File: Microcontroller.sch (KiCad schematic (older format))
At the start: 29 parts, among them J3 USB_B, J4 SWD, J5 DEBUG, U3 STM32F401VETx, U4 USBUF02W6, Y1 8MHz

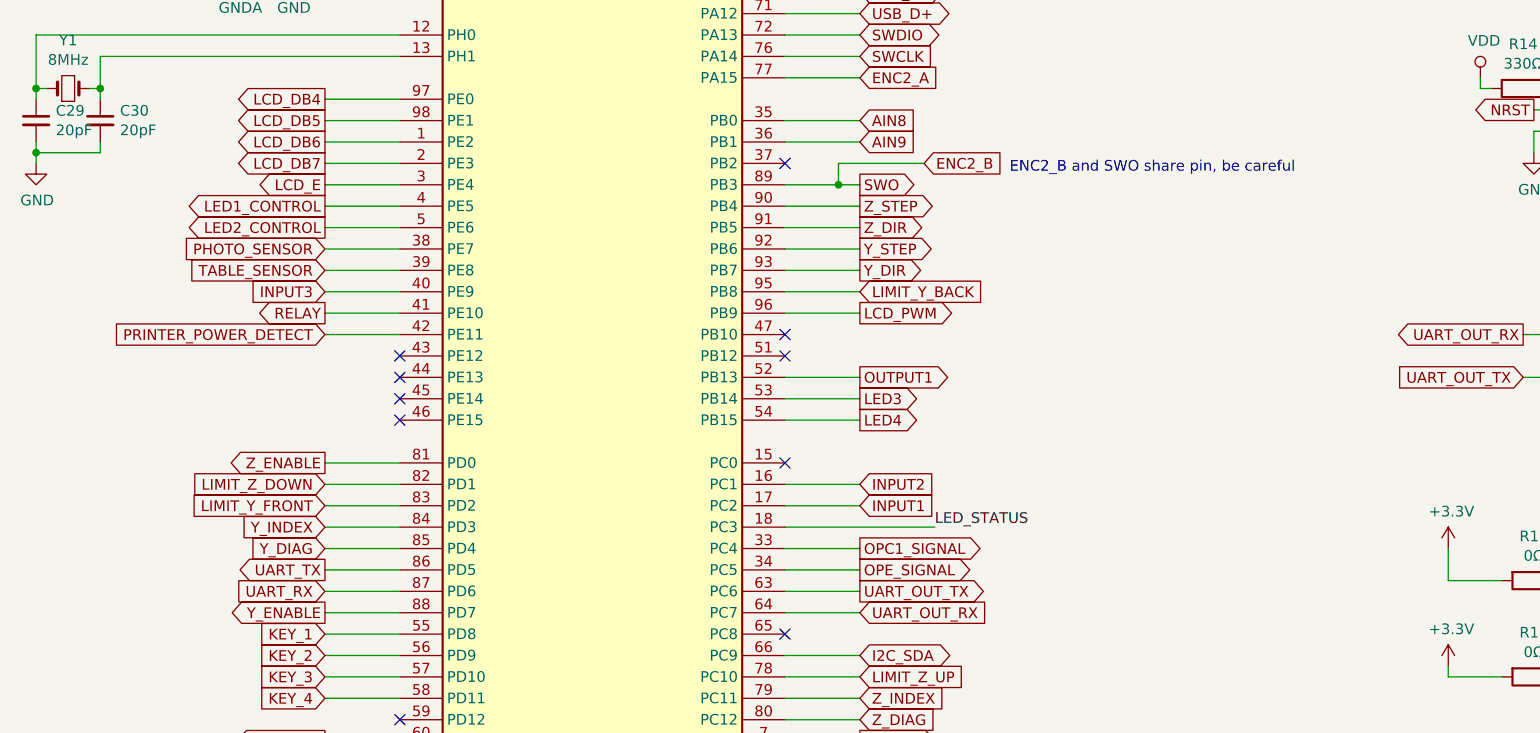
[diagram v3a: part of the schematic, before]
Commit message: Routing emergnency, photo barier, relay, voltage detect, analog, footprint improvment
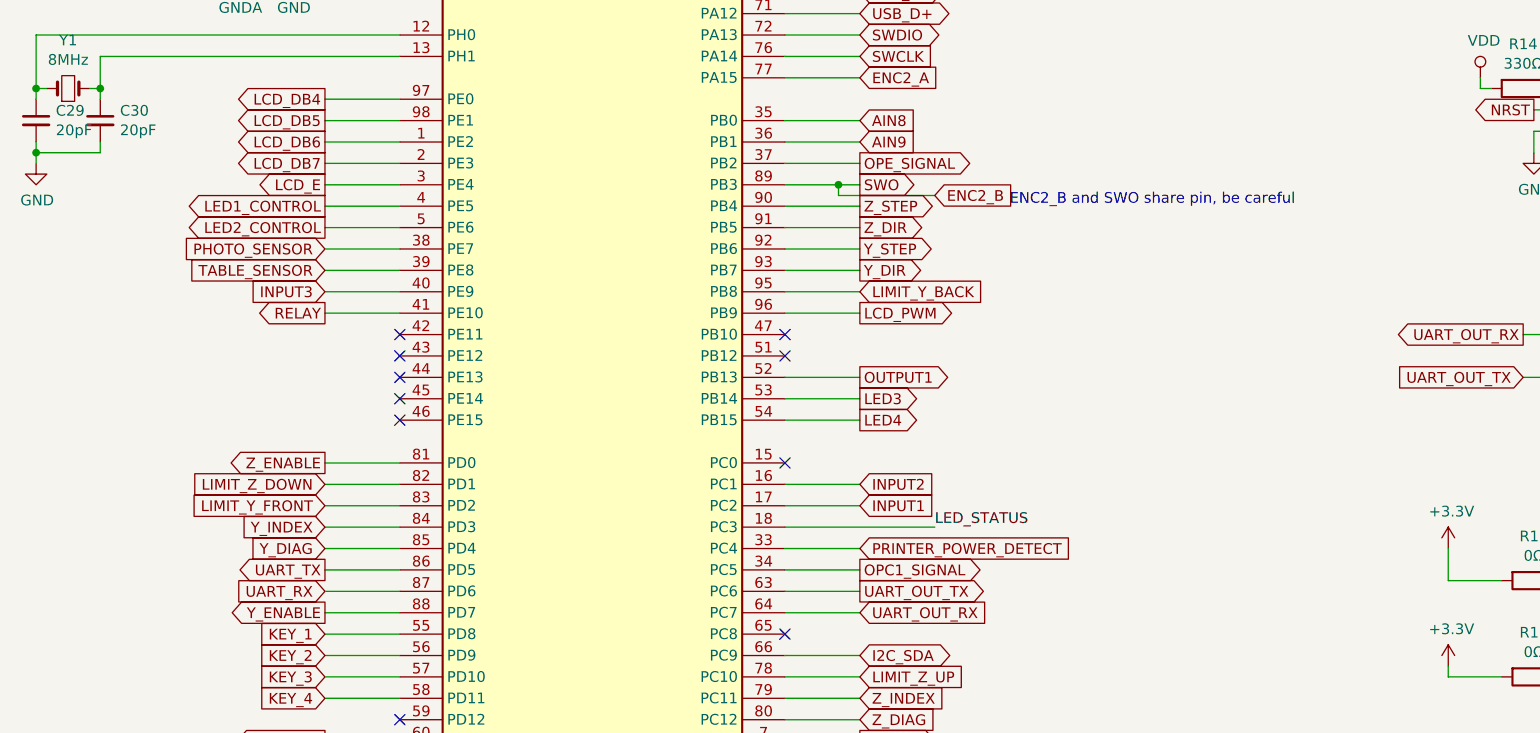
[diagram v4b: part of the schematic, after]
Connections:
- net OPC1_SIGNAL: now also U3.34 (PC5); no longer U3.33 (PC4)
- net OPE_SIGNAL: now also U3.37 (PB2); no longer U3.34 (PC5)
- net PRINTER_POWER_DETECT: now also U3.33 (PC4); no longer U3.42 (PE11)
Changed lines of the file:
@@
 Text GLabel 2500 5050 0    50   Input ~ 0
 LIMIT_Y_FRONT
-Text GLabel 5000 5350 2    50   Output ~ 0
+Text GLabel 5000 3450 2    50   Output ~ 0
 OPE_SIGNAL
 Text GLabel 2500 3850 0    50   Input ~ 0
@@
 	2850 4150 2500 4150
 Wire Wire Line
-	2500 4250 2850 4250
-Wire Wire Line
 	5000 1750 4650 1750
 Wire Wire Line
@@
 Wire Wire Line
 	4650 6150 5000 6150
-Text GLabel 2500 4250 0    50   Input ~ 0
+Text GLabel 5000 5250 2    50   Input ~ 0
 PRINTER_POWER_DETECT
 $Comp
@@
 NoConn ~ 4650 2450
 NoConn ~ 4650 2550
-NoConn ~ 4650 3450
 NoConn ~ 4650 4250
 NoConn ~ 4650 5650
@@
 Text GLabel 5000 3550 2    50   Output ~ 0
 SWO
-Wire Wire Line
-	4650 3550 4900 3550
 Wire Wire Line
 	2750 2050 2750 2250
@@
 Text GLabel 5000 1850 2    50   Input ~ 0
 12V_DETECT
-Text GLabel 5000 5250 2    50   Output ~ 0
+Text GLabel 5000 5350 2    50   Output ~ 0
 OPC1_SIGNAL
 Wire Wire Line
@@
 Text GLabel 5000 3050 2    50   Input ~ 0
 ENC2_A
-Text GLabel 5300 3450 2    50   Input ~ 0
+Text GLabel 5350 3600 2    50   Input ~ 0
 ENC2_B
 Wire Wire Line
 	4650 3050 5000 3050
-Wire Wire Line
-	4900 3550 4900 3450
-Wire Wire Line
-	4900 3450 5300 3450
-Connection ~ 4900 3550
-Wire Wire Line
-	4900 3550 5000 3550
-Text Notes 5700 3500 0    50   ~ 0
+Text Notes 5700 3650 0    50   ~ 0
 ENC2_B and SWO share pin, be careful
 Wire Wire Line
@@
 NoConn ~ 2850 6050
 NoConn ~ 6000 2600
+Wire Wire Line
+	5000 3450 4650 3450
+Wire Wire Line
+	4650 3550 4900 3550
+Wire Wire Line
+	4900 3600 4900 3550
+Connection ~ 4900 3550
+Wire Wire Line
+	4900 3550 5000 3550
+Wire Wire Line
+	4900 3600 5350 3600
+NoConn ~ 2850 4250
 $EndSCHEMATC

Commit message: Routing almost finished
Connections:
- net UART_OUT_RX: now also J5.3 (Pin_3); no longer J5.1 (Pin_1)
- net UART_OUT_TX: now also J5.1 (Pin_1); no longer J5.3 (Pin_3)
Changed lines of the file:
@@
 	-1   0    0    -1
 $EndComp
-Text GLabel 8100 4450 0    50   Input ~ 0
+Text GLabel 8100 4250 0    50   Input ~ 0
 UART_OUT_TX
-Text GLabel 8100 4250 0    50   Output ~ 0
+Text GLabel 8100 4450 0    50   Output ~ 0
 UART_OUT_RX
 Wire Wire Line

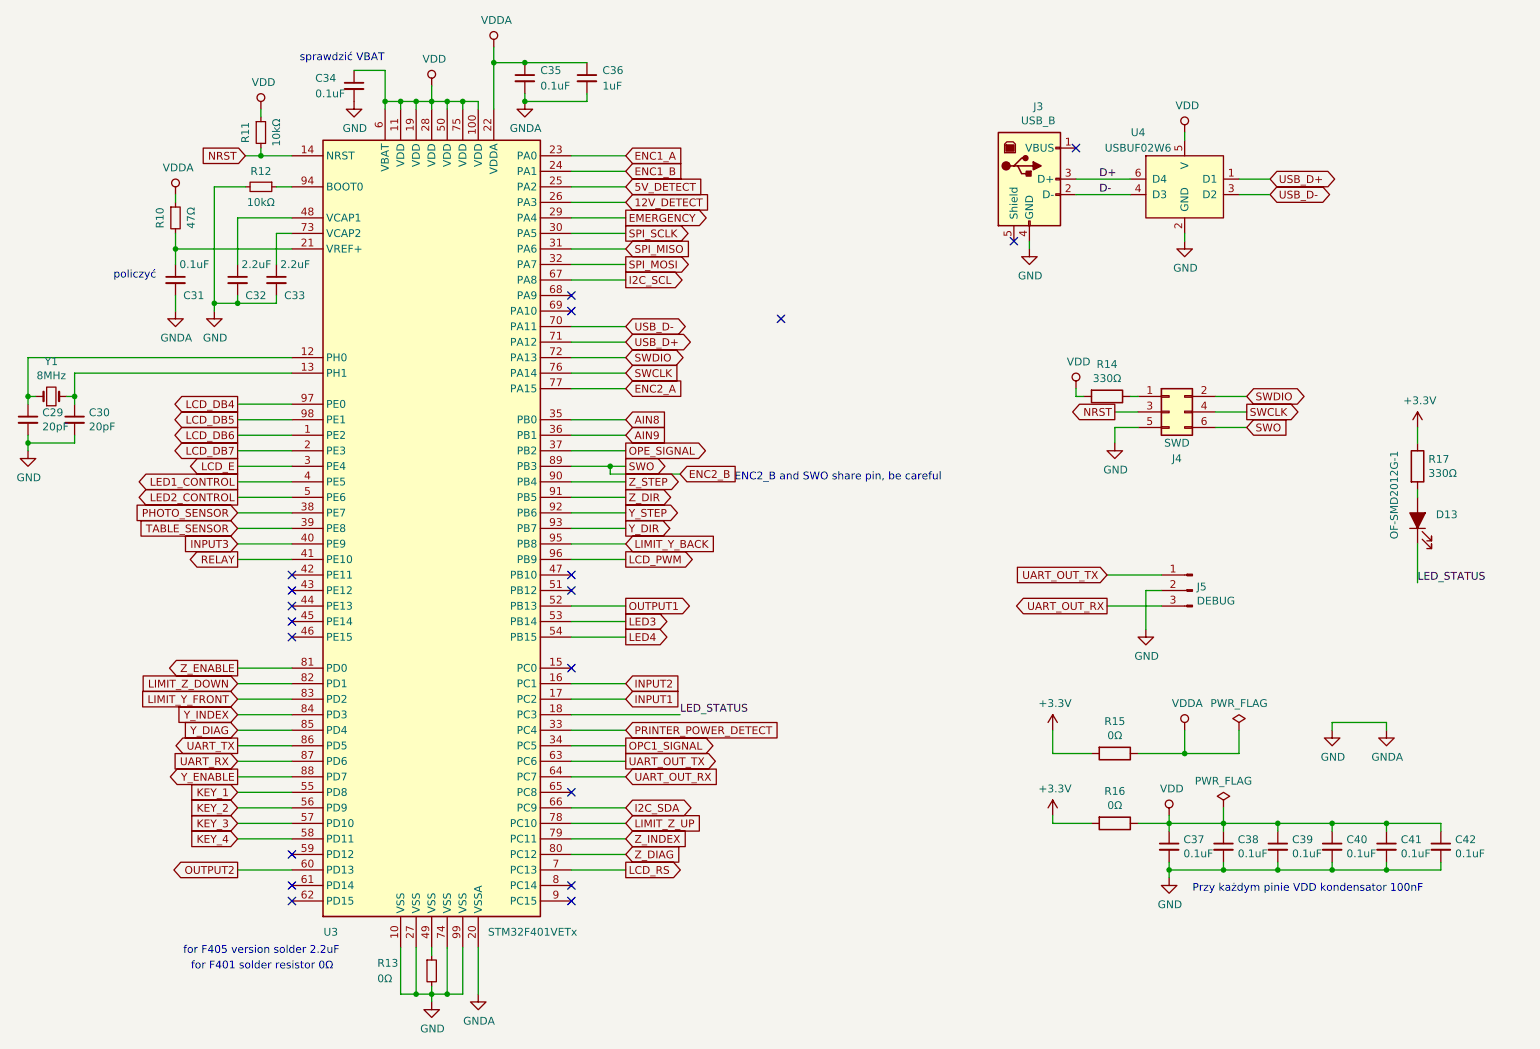
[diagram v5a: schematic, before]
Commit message: Test points, start power plane routing, little change on schematic
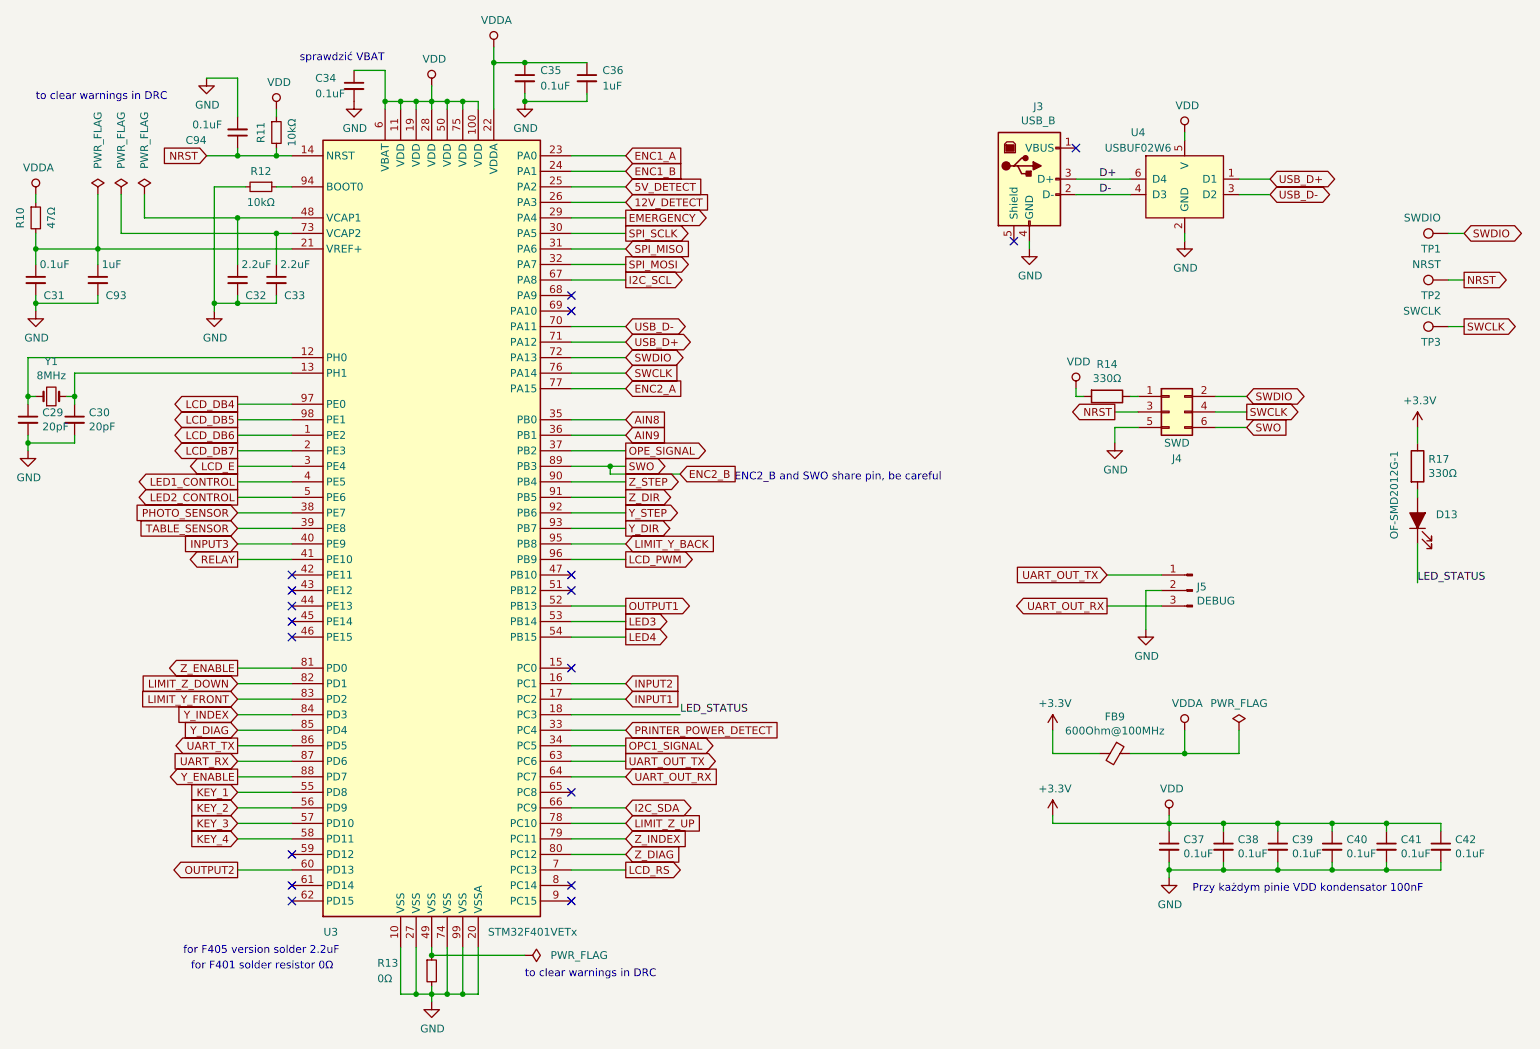
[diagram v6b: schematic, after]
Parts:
- removed R15, R16: 0Ω, Resistor_SMD:R_0603_1608Metric, symbol Device:R
- added C93: 1uF, Capacitor_SMD:C_0603_1608Metric, symbol Device:C_Small
- added C94: 0.1uF, Capacitor_SMD:C_0603_1608Metric, symbol Device:C_Small
- added FB9: 600Ohm@100MHz, Inductor_SMD:L_0603_1608Metric, symbol Device:Ferrite_Bead_Small
- added TP1: SWDIO, TestPoint:TestPoint_Pad_D1.5mm, symbol Connector:TestPoint
- added TP2: NRST, TestPoint:TestPoint_Pad_D1.5mm, symbol Connector:TestPoint
- added TP3: SWCLK, TestPoint:TestPoint_Pad_D1.5mm, symbol Connector:TestPoint
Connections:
- net VDD is gone; now on net +3V3: C34.1, C37.1, C38.1, C39.1, C40.1, C41.1, C42.1, R11.1, R14.2, U3.100 (VDD), U3.11 (VDD), U3.19 (VDD), U3.28 (VDD), U3.50 (VDD), U3.6 (VBAT), U3.75 (VDD), U4.5 (V)
- net +3V3: now also FB9.2
- net GND: now also C93.2, C94.2
- net NRST: now also C94.1, TP2.1
- net SWCLK: now also TP3.1
- net SWDIO: now also TP1.1
- net VDDA: now also FB9.1
- net at C31.1, R10.2, U3.21 (VREF+): now also C93.1
- no-connect marks 19 -> 18
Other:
- note added: "to clear warnings in DRC"
- note removed: "policzyć"
- moved on the sheet: C31, R10, R11

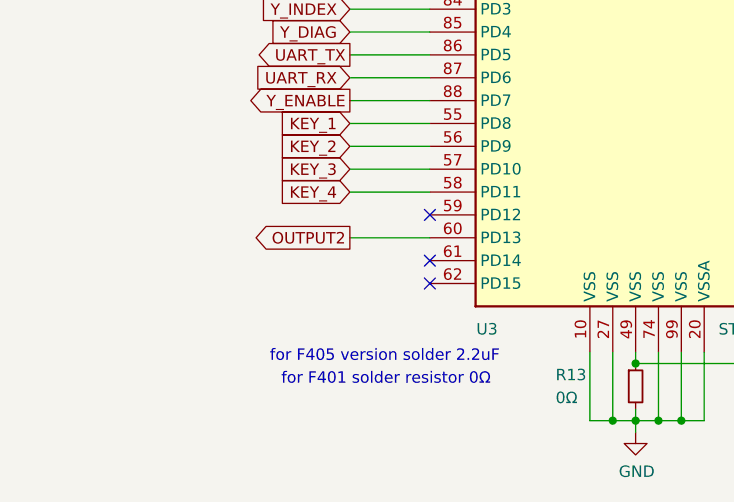
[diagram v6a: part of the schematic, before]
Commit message: Added EEPROM on schematic
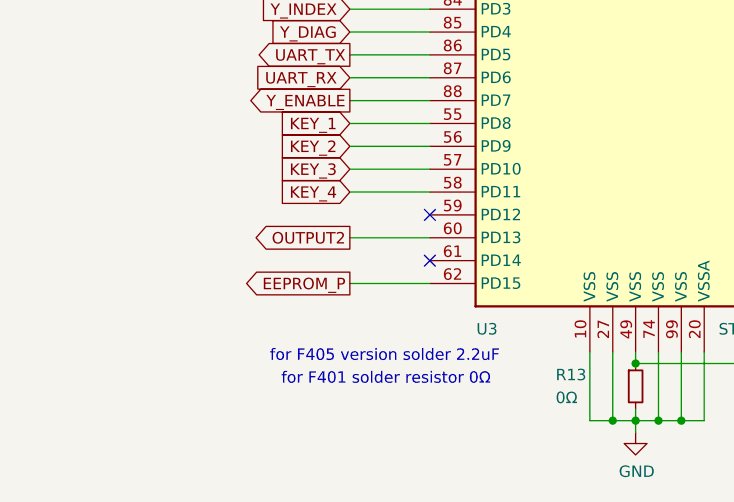
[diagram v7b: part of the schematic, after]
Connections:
- net EEPROM_P: now reaches U3.62 (PD15)
- no-connect marks 18 -> 17
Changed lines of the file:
@@
 NoConn ~ 2850 4650
 NoConn ~ 2850 6250
-NoConn ~ 2850 6350
 Wire Wire Line
 	4650 4450 5000 4450
@@
 $EndComp
 Connection ~ 4350 1200
+Text GLabel 2500 6350 0    50   Output ~ 0
+EEPROM_P
+Wire Wire Line
+	2500 6350 2850 6350
 $EndSCHEMATC

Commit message: Update elements value
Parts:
- C93: Cena 0.08 -> 0.09; Dielektryk (none) -> X7R
- J4: Cena (none) -> 0
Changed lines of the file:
@@
 F 2 "Connector:Tag-Connect_TC2030-IDC-NL_2x03_P1.27mm_Vertical" H 8500 3200 50  0001 C CNN
 F 3 "~" H 8500 3200 50  0001 C CNN
-F 4 "" H 8500 3200 50  0001 C CNN "Cena"
+F 4 "0" H 8500 3200 50  0001 C CNN "Cena"
 F 5 "" H 8500 3200 50  0001 C CNN "Link"
 F 6 "" H 8500 3200 50  0001 C CNN "Model"
@@
 F 2 "Capacitor_SMD:C_0603_1608Metric" H 1600 2350 50  0001 C CNN
 F 3 "~" H 1600 2350 50  0001 C CNN
-F 4 "0.08" H 1600 2350 50  0001 C CNN "Cena"
+F 4 "0.09" H 1600 2350 50  0001 C CNN "Cena"
 F 5 "" H 1600 2350 50  0001 C CNN "Link"
 F 6 "" H 1600 2350 50  0001 C CNN "Model"
@@
 F 8 "" H 1600 2350 50  0001 C CNN "Producent"
 F 9 "SMD" H 1600 2350 50  0001 C CNN "Typ"
+F 10 "X7R" H 1600 2350 50  0001 C CNN "Dielektryk"
 	1    1600 2350
 	1    0    0    -1
